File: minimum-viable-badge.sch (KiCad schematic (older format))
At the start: 42 parts, among them P1 BATTERY, P10 T4, P11 T0, P12 T1, P13 OLED_SPI, P2 USB, P3 CONN_01X14, P4 eInk, P5 CONN_01X10, P6 T7, P7 T6, P8 CONN_01X14, P9 T5, Q1 S8050, Q2 S8050, SW1 PRGM, SW2 RESET, U1 CP2102, U2 ESP32-WROOM

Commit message: Updated cap sense.
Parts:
- removed C10, C5, C6, C7, C8, C9: C, Capacitors_SMD:C_0603_HandSoldering, symbol C
- removed P10: T4, libs:button_arrow, symbol CONN_01X01
- removed P11: T0, libs:button_round, symbol CONN_01X01
- removed P12: T1, libs:button_round, symbol CONN_01X01
- removed P13: OLED_SPI, Pin_Headers:Pin_Header_Straight_1x08_Pitch2.54mm, symbol CONN_01X08
- removed P6: T7, libs:button_arrow, symbol CONN_01X01
- removed P7: T6, libs:button_arrow, symbol CONN_01X01
- removed P9: T5, libs:button_arrow, symbol CONN_01X01
- added P10: POT_4, libs:sense_pot, symbol CONN_01X02
- added P6: POT_1, libs:sense_pot, symbol CONN_01X02
- added P7: POT_2, libs:sense_pot, symbol CONN_01X02
- added P9: POT_3, libs:sense_pot, symbol CONN_01X02
- added R13, R14, R16, R17, R18, R20: 100, Resistors_SMD:R_0603_HandSoldering, symbol R
- P3, P8: footprint Pin_Headers:Pin_Header_Straight_1x14_Pitch2.54mm -> (none)
- P5: footprint Pin_Headers:Pin_Header_Straight_1x10_Pitch2.54mm -> (none)
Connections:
- net labels added: T2
- net labels removed: T7
- wire segments 175 -> 174
- no-connect marks 21 -> 20

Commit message: More pcb work
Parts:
- added P11, P12, P13: MECH, Mounting_Holes:MountingHole_3.2mm_M3_Pad, symbol CONN_01X01
- C1: footprint Capacitors_SMD:C_0603_HandSoldering -> Capacitors_SMD:C_0805_HandSoldering
- P4: footprint (none) -> libs:FPC_0.5mm_Pitch_24_Pin
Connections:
- no-connect marks 20 -> 23
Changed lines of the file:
@@
 F 0 "C1" H 2875 6750 50  0000 L CNN
 F 1 "10uF" H 2875 6550 50  0000 L CNN
-F 2 "Capacitors_SMD:C_0603_HandSoldering" H 2888 6500 50  0001 C CNN
+F 2 "Capacitors_SMD:C_0805_HandSoldering" H 2888 6500 50  0001 C CNN
 F 3 "" H 2850 6650 50  0000 C CNN
 	1    2850 6650
@@
 F 0 "P4" H 5950 6650 50  0000 C CNN
 F 1 "eInk" V 6050 5400 50  0000 C CNN
-F 2 "" H 5950 5400 50  0001 C CNN
+F 2 "libs:FPC_0.5mm_Pitch_24_Pin" H 5950 5400 50  0001 C CNN
 F 3 "" H 5950 5400 50  0000 C CNN
 	1    5950 5400
@@
 Text Label 6400 5350 2    60   ~ 0
 SCLK
+Text Label 6400 5450 2    60   ~ 0
+D/C
 Text Label 6400 5550 2    60   ~ 0
-D/C
+RST
 Text Label 6400 5650 2    60   ~ 0
-RST
-Text Label 6400 5450 2    60   ~ 0
 CS
 Wire Wire Line
@@
 	9250 5450 9200 5450
 Connection ~ 9250 5450
+$Comp
+L CONN_01X01 P13
+U 1 1 5937F8C7
+P 3700 2800
+F 0 "P13" H 3700 2900 50  0000 C CNN
+F 1 "MECH" V 3800 2800 50  0000 C CNN
+F 2 "Mounting_Holes:MountingHole_3.2mm_M3_Pad" H 3700 2800 50  0001 C CNN
+F 3 "" H 3700 2800 50  0000 C CNN
+	1    3700 2800
+	0    -1   -1   0
+$EndComp
+NoConn ~ 3700 3000
+$Comp
+L CONN_01X01 P11
+U 1 1 593802FC
+P 3450 2800
+F 0 "P11" H 3450 2900 50  0000 C CNN
+F 1 "MECH" V 3550 2800 50  0000 C CNN
+F 2 "Mounting_Holes:MountingHole_3.2mm_M3_Pad" H 3450 2800 50  0001 C CNN
+F 3 "" H 3450 2800 50  0000 C CNN
+	1    3450 2800
+	0    -1   -1   0
+$EndComp
+NoConn ~ 3450 3000
+$Comp
+L CONN_01X01 P12
+U 1 1 593803BC
+P 3450 3200
+F 0 "P12" H 3450 3300 50  0000 C CNN
+F 1 "MECH" V 3550 3200 50  0000 C CNN
+F 2 "Mounting_Holes:MountingHole_3.2mm_M3_Pad" H 3450 3200 50  0001 C CNN
+F 3 "" H 3450 3200 50  0000 C CNN
+	1    3450 3200
+	0    -1   -1   0
+$EndComp
+NoConn ~ 3450 3400
 $EndSCHEMATC

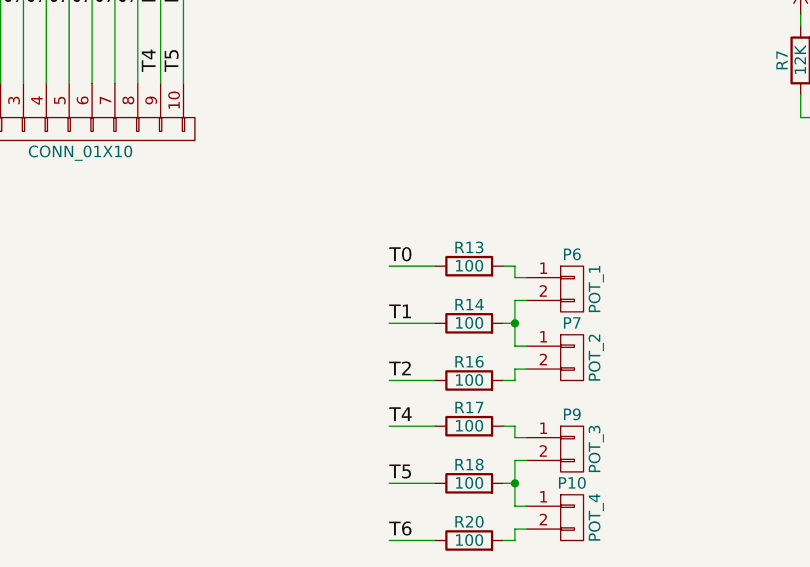
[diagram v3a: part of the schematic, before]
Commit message: Updated pcb layout.
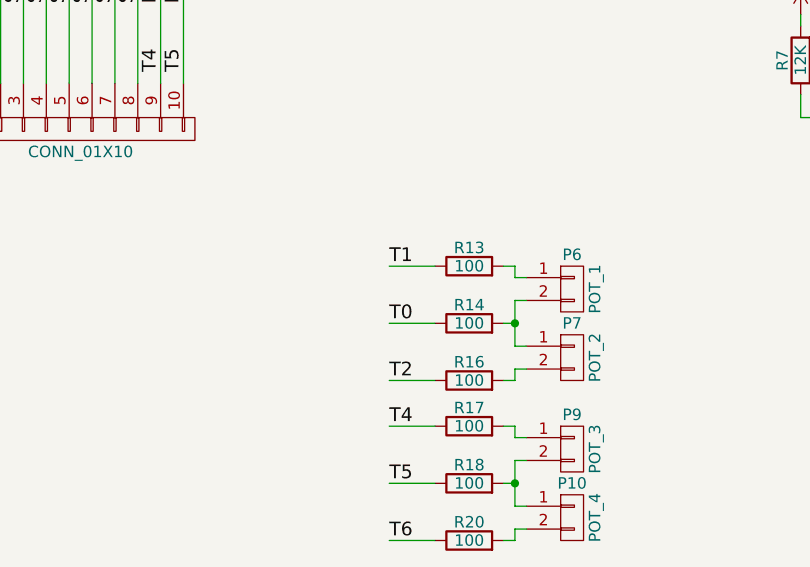
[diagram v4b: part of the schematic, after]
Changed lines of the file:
@@
 Text Label 5750 2500 0    60   ~ 0
 T1
+Text Label 8700 4750 0    60   ~ 0
+T0
 Text Label 8700 4500 0    60   ~ 0
-T0
-Text Label 8700 4750 0    60   ~ 0
 T1
 $Comp

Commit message: Damnit.  S8050 backwards
Thanks https://github.com/rdpowers.  Fixes #2
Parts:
- removed Q1, Q2: S8050, TO_SOT_Packages_SMD:SOT-23_Handsoldering, symbol S8050
- added Q1, Q2: S8050, TO_SOT_Packages_SMD:SOT-23_Handsoldering, symbol Q_NPN_BEC
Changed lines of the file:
@@
 $EndComp
 $Comp
-L +3.3V #PWR01
+L +3.3V #PWR12
 U 1 1 592724E6
 P 6300 1200
-F 0 "#PWR01" H 6300 1050 50  0001 C CNN
+F 0 "#PWR12" H 6300 1050 50  0001 C CNN
 F 1 "+3.3V" H 6300 1340 50  0000 C CNN
 F 2 "" H 6300 1200 50  0000 C CNN
@@
 SENSOR_VP
 $Comp
-L GND #PWR02
+L GND #PWR13
 U 1 1 59273E9D
 P 6300 3150
-F 0 "#PWR02" H 6300 2900 50  0001 C CNN
+F 0 "#PWR13" H 6300 2900 50  0001 C CNN
 F 1 "GND" H 6300 3000 50  0000 C CNN
 F 2 "" H 6300 3150 50  0000 C CNN
@@
 	7500 2950 7500 3700
 $Comp
-L GND #PWR03
+L GND #PWR16
 U 1 1 5926EF0D
 P 8400 2700
-F 0 "#PWR03" H 8400 2450 50  0001 C CNN
+F 0 "#PWR16" H 8400 2450 50  0001 C CNN
 F 1 "GND" H 8400 2550 50  0000 C CNN
 F 2 "" H 8400 2700 50  0000 C CNN
@@
 $EndComp
 $Comp
-L GND #PWR04
+L GND #PWR18
 U 1 1 59270E7E
 P 10150 1550
-F 0 "#PWR04" H 10150 1300 50  0001 C CNN
+F 0 "#PWR18" H 10150 1300 50  0001 C CNN
 F 1 "GND" H 10150 1400 50  0000 C CNN
 F 2 "" H 10150 1550 50  0000 C CNN
@@
 $EndComp
 $Comp
-L GND #PWR05
+L GND #PWR19
 U 1 1 59271D6E
 P 10150 2750
-F 0 "#PWR05" H 10150 2500 50  0001 C CNN
+F 0 "#PWR19" H 10150 2500 50  0001 C CNN
 F 1 "GND" H 10150 2600 50  0000 C CNN
 F 2 "" H 10150 2750 50  0000 C CNN
@@
 $EndComp
 $Comp
-L +3.3V #PWR06
+L +3.3V #PWR20
 U 1 1 59272070
 P 10500 3400
-F 0 "#PWR06" H 10500 3250 50  0001 C CNN
+F 0 "#PWR20" H 10500 3250 50  0001 C CNN
 F 1 "+3.3V" H 10500 3540 50  0000 C CNN
 F 2 "" H 10500 3400 50  0000 C CNN
@@
 $EndComp
 $Comp
-L GND #PWR07
+L GND #PWR2
 U 1 1 592733B2
 P 1250 1500
-F 0 "#PWR07" H 1250 1250 50  0001 C CNN
+F 0 "#PWR2" H 1250 1250 50  0001 C CNN
 F 1 "GND" H 1250 1350 50  0000 C CNN
 F 2 "" H 1250 1500 50  0000 C CNN
@@
 $EndComp
 $Comp
-L GND #PWR08
+L GND #PWR10
 U 1 1 59278253
 P 3850 7350
-F 0 "#PWR08" H 3850 7100 50  0001 C CNN
+F 0 "#PWR10" H 3850 7100 50  0001 C CNN
 F 1 "GND" H 3850 7200 50  0000 C CNN
 F 2 "" H 3850 7350 50  0000 C CNN
@@
 $EndComp
 $Comp
-L GND #PWR09
+L GND #PWR7
 U 1 1 59278B43
 P 3150 6900
-F 0 "#PWR09" H 3150 6650 50  0001 C CNN
+F 0 "#PWR7" H 3150 6650 50  0001 C CNN
 F 1 "GND" H 3150 6750 50  0000 C CNN
 F 2 "" H 3150 6900 50  0000 C CNN
@@
 Connection ~ 3150 6250
 $Comp
-L +3.3V #PWR010
+L +3.3V #PWR6
 U 1 1 59278F2C
 P 2850 6400
-F 0 "#PWR010" H 2850 6250 50  0001 C CNN
+F 0 "#PWR6" H 2850 6250 50  0001 C CNN
 F 1 "+3.3V" H 2850 6540 50  0000 C CNN
 F 2 "" H 2850 6400 50  0000 C CNN
@@
 	2850 5850 2850 5900
 $Comp
-L GND #PWR011
+L GND #PWR5
 U 1 1 5927A61E
 P 2850 5900
-F 0 "#PWR011" H 2850 5650 50  0001 C CNN
+F 0 "#PWR5" H 2850 5650 50  0001 C CNN
 F 1 "GND" H 2850 5750 50  0000 C CNN
 F 2 "" H 2850 5900 50  0000 C CNN
@@
 DTR
 $Comp
-L GND #PWR012
+L GND #PWR8
 U 1 1 5927C255
 P 3600 5150
-F 0 "#PWR012" H 3600 4900 50  0001 C CNN
+F 0 "#PWR8" H 3600 4900 50  0001 C CNN
 F 1 "GND" H 3600 5000 50  0000 C CNN
 F 2 "" H 3600 5150 50  0000 C CNN
@@
 Wire Wire Line
 	3600 5050 3800 5050
-$Comp
-L S8050 Q1
-U 1 1 5927CABD
-P 1950 5900
-F 0 "Q1" H 2150 5975 50  0000 L CNN
-F 1 "S8050" H 2150 5900 50  0000 L CNN
-F 2 "TO_SOT_Packages_SMD:SOT-23_Handsoldering" V 2500 5750 50  0001 L CIN
-F 3 "" H 1950 5900 50  0000 L CNN
-	1    1950 5900
-	1    0    0    -1
-$EndComp
-$Comp
-L S8050 Q2
-U 1 1 5927CB5A
-P 1950 6600
-F 0 "Q2" H 2150 6675 50  0000 L CNN
-F 1 "S8050" H 2150 6600 50  0000 L CNN
-F 2 "TO_SOT_Packages_SMD:SOT-23_Handsoldering" H 950 7050 50  0001 L CIN
-F 3 "" H 1950 6600 50  0000 L CNN
-	1    1950 6600
-	1    0    0    1
-$EndComp
 $Comp
 L R R4
@@
 	1800 4000 1800 4100
 $Comp
-L GND #PWR013
+L GND #PWR3
 U 1 1 592802B0
 P 1800 4100
-F 0 "#PWR013" H 1800 3850 50  0001 C CNN
+F 0 "#PWR3" H 1800 3850 50  0001 C CNN
 F 1 "GND" H 1800 3950 50  0000 C CNN
 F 2 "" H 1800 4100 50  0000 C CNN
@@
 $EndComp
 $Comp
-L GND #PWR014
+L GND #PWR1
 U 1 1 592812C4
 P 1150 2800
-F 0 "#PWR014" H 1150 2550 50  0001 C CNN
+F 0 "#PWR1" H 1150 2550 50  0001 C CNN
 F 1 "GND" H 1150 2650 50  0000 C CNN
 F 2 "" H 1150 2800 50  0000 C CNN
@@
 $EndComp
 $Comp
-L GND #PWR015
+L GND #PWR4
 U 1 1 59281D15
 P 1900 3100
-F 0 "#PWR015" H 1900 2850 50  0001 C CNN
+F 0 "#PWR4" H 1900 2850 50  0001 C CNN
 F 1 "GND" H 1900 2950 50  0000 C CNN
 F 2 "" H 1900 3100 50  0000 C CNN
@@
 $EndSheet
 $Comp
-L +3.3V #PWR016
+L +3.3V #PWR9
 U 1 1 59288975
 P 3850 1350
-F 0 "#PWR016" H 3850 1200 50  0001 C CNN
+F 0 "#PWR9" H 3850 1200 50  0001 C CNN
 F 1 "+3.3V" H 3850 1490 50  0000 C CNN
 F 2 "" H 3850 1350 50  0000 C CNN
@@
 $EndComp
 $Comp
-L GND #PWR017
+L GND #PWR17
 U 1 1 59294F03
 P 8800 800
-F 0 "#PWR017" H 8800 550 50  0001 C CNN
+F 0 "#PWR17" H 8800 550 50  0001 C CNN
 F 1 "GND" H 8800 650 50  0000 C CNN
 F 2 "" H 8800 800 50  0000 C CNN
@@
 Connection ~ 6300 1300
 $Comp
-L GND #PWR018
+L GND #PWR11
 U 1 1 59297E2A
 P 5800 1050
-F 0 "#PWR018" H 5800 800 50  0001 C CNN
+F 0 "#PWR11" H 5800 800 50  0001 C CNN
 F 1 "GND" H 5800 900 50  0000 C CNN
 F 2 "" H 5800 1050 50  0000 C CNN
@@
 	6150 4950 6650 4950
 $Comp
-L GND #PWR019
+L GND #PWR15
 U 1 1 592DE146
 P 6650 5000
-F 0 "#PWR019" H 6650 4750 50  0001 C CNN
+F 0 "#PWR15" H 6650 4750 50  0001 C CNN
 F 1 "GND" H 6650 4850 50  0000 C CNN
 F 2 "" H 6650 5000 50  0000 C CNN
@@
 Connection ~ 6400 5050
 $Comp
-L +3.3V #PWR020
+L +3.3V #PWR14
 U 1 1 592DF2FA
 P 6400 4700
-F 0 "#PWR020" H 6400 4550 50  0001 C CNN
+F 0 "#PWR14" H 6400 4550 50  0001 C CNN
 F 1 "+3.3V" H 6400 4840 50  0000 C CNN
 F 2 "" H 6400 4700 50  0000 C CNN
@@
 $EndComp
 NoConn ~ 3450 3400
+$Comp
+L Q_NPN_BEC Q1
+U 1 1 593FEB64
+P 1950 5900
+F 0 "Q1" H 2250 5950 50  0000 R CNN
+F 1 "S8050" H 2400 5850 50  0000 R CNN
+F 2 "TO_SOT_Packages_SMD:SOT-23_Handsoldering" H 2150 6000 50  0001 C CNN
+F 3 "" H 1950 5900 50  0000 C CNN
+F 4 "MMSS8050-H-TPMSCT-ND" H 1950 5900 60  0001 C CNN "Digikey PN"
+F 5 "http://www.digikey.com.au/product-detail/en/micro-commercial-co/MMSS8050-H-TP/MMSS8050-H-TPMSCT-ND/2825945" H 1950 5900 60  0001 C CNN "Link"
+F 6 "MMSS8050-H-TP" H 1950 5900 60  0001 C CNN "Manufacture PN"
+F 7 "0.20" H 1950 5900 60  0001 C CNN "Cost"
+	1    1950 5900
+	1    0    0    -1
+$EndComp
+$Comp
+L Q_NPN_BEC Q2
+U 1 1 593FF3B5
+P 1950 6600
+F 0 "Q2" H 2250 6650 50  0000 R CNN
+F 1 "S8050" H 2400 6550 50  0000 R CNN
+F 2 "TO_SOT_Packages_SMD:SOT-23_Handsoldering" H 2150 6700 50  0001 C CNN
+F 3 "" H 1950 6600 50  0000 C CNN
+	1    1950 6600
+	1    0    0    1
+$EndComp
 $EndSCHEMATC

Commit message: Added some digikey links.
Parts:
- C1, C3: Digikey PN (none) -> 1276-2399-1-ND; Link (none) -> http://www.digikey.com.au/product-detail/en/samsung-electro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; Manufacturer PN (none) -> CL21A106KOCLRNC; Unit Cost (none) -> 0.18
- C2, C4: Digikey PN (none) -> 311-1088-1-ND; Link (none) -> http://www.digikey.com.au/product-detail/en/yageo/CC0603KRX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; Manufacturer PN (none) -> CC0603KRX7R7BB104; Unit Cost (none) -> 0.10
- D1: Digikey PN (none) -> SS14CT-ND; Link (none) -> http://www.digikey.com.au/product-detail/en/fairchild-semic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; Manufacturer PN (none) -> SS14; Unit Cost (none) -> 0.39
- F1: Digikey PN (none) -> 507-1786-1-ND; Link (none) -> http://www.digikey.com.au/product-detail/en/bel-fuse-inc/0Z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; Manufacturer PN (none) -> 0ZCH0050FF2G; Unit Cost (none) -> 0.12
- P2: Digikey PN (none) -> 609-4618-1-ND; Link (none) -> http://www.digikey.com.au/product-detail/en/amphenol-fci/10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; Manufacturer PN (none) -> 10118194-0001LF; Unit Cost (none) -> 0.46
- Q2: Cost (none) -> 0.20; Digikey PN (none) -> MMSS8050-H-TPMSCT-ND; Link (none) -> http://www.digikey.com.au/product-detail/en/micro-commercia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; Manufacture PN (none) -> MMSS8050-H-TP
- R1: Digikey PN (none) -> 311-1.00MHRCT-ND; Link (none) -> http://www.digikey.com.au/product-detail/en/yageo/RC0603FR-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; Manufacturer PN (none) -> RC0603FR-071ML; Unit Cost (none) -> 0.10
- R2: Digikey PN (none) -> 311-100KGRCT-ND; Link (none) -> http://www.digikey.com.au/product-detail/en/yageo/RC0603JR-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; Manufacturer PN (none) -> RC0603JR-07100KL; Unit Cost (none) -> 0.10
- R3, R4, R7: Digikey PN (none) -> 311-12.0KHRCT-ND; Link (none) -> http://www.digikey.com.au/product-detail/en/yageo/RC0603FR-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; Manufacturer PN (none) -> RC0603FR-0712KL; Unit Cost (none) -> 0.10
- R5: Digikey PN (none) -> 311-10KGRCT-ND; Link (none) -> http://www.digikey.com.au/product-detail/en/yageo/RC0603JR-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; Manufacturer PN (none) -> RC0603JR-0710KL; Unit Cost (none) -> 0.10
- R6, R8, R9: Digikey PN (none) -> 311-470HRCT-ND; Link (none) -> http://www.digikey.com.au/product-detail/en/yageo/RC0603FR-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; Manufacturer PN (none) -> RC0603FR-07470RL; Unit Cost (none) -> 0.10
- U1: Digikey PN (none) -> 336-1160-1-ND; Link (none) -> http://www.digikey.com.au/product-detail/en/silicon-labs/CP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; Manufacturer PN (none) -> CP2102-GMR; Unit Cost (none) -> 2.88
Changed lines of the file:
@@
 F 2 "Resistors_SMD:R_0603_HandSoldering" V 10630 800 50  0001 C CNN
 F 3 "" H 10700 800 50  0000 C CNN
+F 4 "311-470HRCT-ND" V 10800 800 60  0001 C CNN "Digikey PN"
+F 5 "http://www.digikey.com.au/product-detail/en/yageo/RC0603FR-07470RL/311-470HRCT-ND/730203" V 10800 800 60  0001 C CNN "Link"
+F 6 "RC0603FR-07470RL" V 10800 800 60  0001 C CNN "Manufacturer PN"
+F 7 "0.10" V 10800 800 60  0001 C CNN "Unit Cost"
 	1    10700 800
 	0    1    1    0
@@
 F 2 "Resistors_SMD:R_0603_HandSoldering" V 10630 2000 50  0001 C CNN
 F 3 "" H 10700 2000 50  0000 C CNN
+F 4 "311-470HRCT-ND" V 10800 800 60  0001 C CNN "Digikey PN"
+F 5 "http://www.digikey.com.au/product-detail/en/yageo/RC0603FR-07470RL/311-470HRCT-ND/730203" V 10800 800 60  0001 C CNN "Link"
+F 6 "RC0603FR-07470RL" V 10800 800 60  0001 C CNN "Manufacturer PN"
+F 7 "0.10" V 10800 800 60  0001 C CNN "Unit Cost"
 	1    10700 2000
 	0    1    1    0
@@
 F 2 "Resistors_SMD:R_0603_HandSoldering" V 10430 3600 50  0001 C CNN
 F 3 "" H 10500 3600 50  0000 C CNN
+F 4 "311-12.0KHRCT-ND" V 1100 5000 60  0001 C CNN "Digikey PN"
+F 5 "http://www.digikey.com.au/product-detail/en/yageo/RC0603FR-0712KL/311-12.0KHRCT-ND/729860" V 1100 5000 60  0001 C CNN "Link"
+F 6 "RC0603FR-0712KL" V 1100 5000 60  0001 C CNN "Manufacturer PN"
+F 7 "0.10" V 1100 5000 60  0001 C CNN "Unit Cost"
 	1    10500 3600
 	-1   0    0    1
@@
 F 2 "libs:USB-MICRO-5pin_PTHMOUNT-Amphenol.10118194-0001LF" V 850 850 50  0001 C CNN
 F 3 "" V 850 850 50  0000 C CNN
+F 4 "609-4618-1-ND" H 950 1800 60  0001 C CNN "Digikey PN"
+F 5 "http://www.digikey.com.au/product-detail/en/amphenol-fci/10118194-0001LF/609-4618-1-ND/2785382" H 950 1800 60  0001 C CNN "Link"
+F 6 "10118194-0001LF" H 950 1800 60  0001 C CNN "Manufacturer PN"
+F 7 "0.46" H 950 1800 60  0001 C CNN "Unit Cost"
 	1    900  950
 	0    -1   1    0
@@
 F 2 "Housings_DFN_QFN:QFN-28-1EP_5x5mm_Pitch0.5mm" H 4150 6000 60  0001 C CNN
 F 3 "" H 4150 6000 60  0000 C CNN
+F 4 "336-1160-1-ND" H 3800 6200 60  0001 C CNN "Digikey PN"
+F 5 "http://www.digikey.com.au/product-detail/en/silicon-labs/CP2102-GMR/336-1160-1-ND/3672615" H 3800 6200 60  0001 C CNN "Link"
+F 6 "CP2102-GMR" H 3800 6200 60  0001 C CNN "Manufacturer PN"
+F 7 "2.88" H 3800 6200 60  0001 C CNN "Unit Cost"
 	1    4150 6000
 	1    0    0    -1
@@
 F 2 "Capacitors_SMD:C_0603_HandSoldering" H 3888 6950 50  0001 C CNN
 F 3 "" H 3850 7100 50  0000 C CNN
+F 4 "311-1088-1-ND" H 2300 6550 60  0001 C CNN "Digikey PN"
+F 5 "http://www.digikey.com.au/product-detail/en/yageo/CC0603KRX7R7BB104/311-1088-1-ND/302998" H 2300 6550 60  0001 C CNN "Link"
+F 6 "CC0603KRX7R7BB104" H 2300 6550 60  0001 C CNN "Manufacturer PN"
+F 7 "0.10" H 2300 6550 60  0001 C CNN "Unit Cost"
 	1    3850 7100
 	1    0    0    -1
@@
 F 2 "Capacitors_SMD:C_0805_HandSoldering" H 3588 6950 50  0001 C CNN
 F 3 "" H 3550 7100 50  0000 C CNN
+F 4 "1276-2399-1-ND" H 1950 6550 60  0001 C CNN "Digikey PN"
+F 5 "http://www.digikey.com.au/product-detail/en/samsung-electro-mechanics-america-inc/CL21A106KOCLRNC/1276-2399-1-ND/3890485" H 1950 6550 60  0001 C CNN "Link"
+F 6 "CL21A106KOCLRNC" H 1950 6550 60  0001 C CNN "Manufacturer PN"
+F 7 "0.18" H 1950 6550 60  0001 C CNN "Unit Cost"
 	1    3550 7100
 	1    0    0    -1
@@
 F 2 "Capacitors_SMD:C_0603_HandSoldering" H 3188 6500 50  0001 C CNN
 F 3 "" H 3150 6650 50  0000 C CNN
+F 4 "311-1088-1-ND" H 2300 6550 60  0001 C CNN "Digikey PN"
+F 5 "http://www.digikey.com.au/product-detail/en/yageo/CC0603KRX7R7BB104/311-1088-1-ND/302998" H 2300 6550 60  0001 C CNN "Link"
+F 6 "CC0603KRX7R7BB104" H 2300 6550 60  0001 C CNN "Manufacturer PN"
+F 7 "0.10" H 2300 6550 60  0001 C CNN "Unit Cost"
 	1    3150 6650
 	1    0    0    -1
@@
 F 2 "Capacitors_SMD:C_0805_HandSoldering" H 2888 6500 50  0001 C CNN
 F 3 "" H 2850 6650 50  0000 C CNN
+F 4 "1276-2399-1-ND" H 1950 6550 60  0001 C CNN "Digikey PN"
+F 5 "http://www.digikey.com.au/product-detail/en/samsung-electro-mechanics-america-inc/CL21A106KOCLRNC/1276-2399-1-ND/3890485" H 1950 6550 60  0001 C CNN "Link"
+F 6 "CL21A106KOCLRNC" H 1950 6550 60  0001 C CNN "Manufacturer PN"
+F 7 "0.18" H 1950 6550 60  0001 C CNN "Unit Cost"
 	1    2850 6650
 	1    0    0    -1
@@
 F 2 "Resistors_SMD:R_0603_HandSoldering" V 4230 4700 50  0001 C CNN
 F 3 "" H 4300 4700 50  0000 C CNN
+F 4 "311-470HRCT-ND" V 10800 800 60  0001 C CNN "Digikey PN"
+F 5 "http://www.digikey.com.au/product-detail/en/yageo/RC0603FR-07470RL/311-470HRCT-ND/730203" V 10800 800 60  0001 C CNN "Link"
+F 6 "RC0603FR-07470RL" V 10800 800 60  0001 C CNN "Manufacturer PN"
+F 7 "0.10" V 10800 800 60  0001 C CNN "Unit Cost"
 	1    4300 4700
 	0    1    1    0
@@
 F 2 "Resistors_SMD:R_0603_HandSoldering" V 1330 6600 50  0001 C CNN
 F 3 "" H 1400 6600 50  0000 C CNN
+F 4 "311-12.0KHRCT-ND" V 1100 5000 60  0001 C CNN "Digikey PN"
+F 5 "http://www.digikey.com.au/product-detail/en/yageo/RC0603FR-0712KL/311-12.0KHRCT-ND/729860" V 1100 5000 60  0001 C CNN "Link"
+F 6 "RC0603FR-0712KL" V 1100 5000 60  0001 C CNN "Manufacturer PN"
+F 7 "0.10" V 1100 5000 60  0001 C CNN "Unit Cost"
 	1    1400 6600
 	0    1    1    0
@@
 F 2 "Resistors_SMD:R_0603_HandSoldering" V 1330 5900 50  0001 C CNN
 F 3 "" H 1400 5900 50  0000 C CNN
+F 4 "311-12.0KHRCT-ND" V 1100 5000 60  0001 C CNN "Digikey PN"
+F 5 "http://www.digikey.com.au/product-detail/en/yageo/RC0603FR-0712KL/311-12.0KHRCT-ND/729860" V 1100 5000 60  0001 C CNN "Link"
+F 6 "RC0603FR-0712KL" V 1100 5000 60  0001 C CNN "Manufacturer PN"
+F 7 "0.10" V 1100 5000 60  0001 C CNN "Unit Cost"
 	1    1400 5900
 	0    1    1    0
@@
 F 2 "Resistors_SMD:R_0603_HandSoldering" V 830 3750 50  0001 C CNN
 F 3 "" H 900 3750 50  0000 C CNN
+F 4 "311-1.00MHRCT-ND" V 700 2850 60  0001 C CNN "Digikey PN"
+F 5 "http://www.digikey.com.au/product-detail/en/yageo/RC0603FR-071ML/311-1.00MHRCT-ND/729791" V 700 2850 60  0001 C CNN "Link"
+F 6 "RC0603FR-071ML" V 700 2850 60  0001 C CNN "Manufacturer PN"
+F 7 "0.10" V 700 2850 60  0001 C CNN "Unit Cost"
 	1    900  3750
 	-1   0    0    1
@@
 F 2 "Resistors_SMD:R_0603_HandSoldering" V 1080 4000 50  0001 C CNN
 F 3 "" H 1150 4000 50  0000 C CNN
+F 4 "311-100KGRCT-ND" V 950 3100 60  0001 C CNN "Digikey PN"
+F 5 "http://www.digikey.com.au/product-detail/en/yageo/RC0603JR-07100KL/311-100KGRCT-ND/729645" V 950 3100 60  0001 C CNN "Link"
+F 6 "RC0603JR-07100KL" V 950 3100 60  0001 C CNN "Manufacturer PN"
+F 7 "0.10" V 950 3100 60  0001 C CNN "Unit Cost"
 	1    1150 4000
 	0    -1   -1   0
@@
 F 2 "Resistors_SMD:R_0603_HandSoldering" V 1480 4000 50  0001 C CNN
 F 3 "" H 1550 4000 50  0000 C CNN
+F 4 "311-10KGRCT-ND" V 1300 3100 60  0001 C CNN "Digikey PN"
+F 5 "http://www.digikey.com.au/product-detail/en/yageo/RC0603JR-0710KL/311-10KGRCT-ND/729647" V 1300 3100 60  0001 C CNN "Link"
+F 6 "RC0603JR-0710KL" V 1300 3100 60  0001 C CNN "Manufacturer PN"
+F 7 "0.10" V 1300 3100 60  0001 C CNN "Unit Cost"
 	1    1550 4000
 	0    -1   -1   0
@@
 F 2 "Diodes_SMD:D_1206" H 1550 2600 50  0001 C CNN
 F 3 "" H 1550 2600 50  0000 C CNN
+F 4 "507-1786-1-ND" H 1650 850 60  0001 C CNN "Digikey PN"
+F 5 "http://www.digikey.com.au/product-detail/en/bel-fuse-inc/0ZCH0050FF2G/507-1786-1-ND/4156209" H 1650 850 60  0001 C CNN "Link"
+F 6 "0ZCH0050FF2G" H 1650 850 60  0001 C CNN "Manufacturer PN"
+F 7 "0.12" H 1650 850 60  0001 C CNN "Unit Cost"
 	1    1550 2600
 	1    0    0    -1
@@
 F 2 "Diodes_SMD:D_SMA" H 1900 2850 50  0001 C CNN
 F 3 "" H 1900 2850 50  0000 C CNN
+F 4 "SS14CT-ND" H 2000 1150 60  0001 C CNN "Digikey PN"
+F 5 "http://www.digikey.com.au/product-detail/en/fairchild-semiconductor/SS14/SS14CT-ND/965729" H 2000 1150 60  0001 C CNN "Link"
+F 6 "SS14" H 2000 1150 60  0001 C CNN "Manufacturer PN"
+F 7 "0.39" H 2000 1150 60  0001 C CNN "Unit Cost"
 	1    1900 2850
 	0    1    1    0
@@
 F 2 "TO_SOT_Packages_SMD:SOT-23_Handsoldering" H 2150 6700 50  0001 C CNN
 F 3 "" H 1950 6600 50  0000 C CNN
+F 4 "MMSS8050-H-TPMSCT-ND" H 1950 5900 60  0001 C CNN "Digikey PN"
+F 5 "http://www.digikey.com.au/product-detail/en/micro-commercial-co/MMSS8050-H-TP/MMSS8050-H-TPMSCT-ND/2825945" H 1950 5900 60  0001 C CNN "Link"
+F 6 "MMSS8050-H-TP" H 1950 5900 60  0001 C CNN "Manufacture PN"
+F 7 "0.20" H 1950 5900 60  0001 C CNN "Cost"
 	1    1950 6600
 	1    0    0    1
